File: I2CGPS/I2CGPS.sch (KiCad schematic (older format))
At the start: 9 parts, among them P1 CONN_01X05, P2 CONN_01X09, P3 CONN_01X09, Q1 BSS84, U1 GY-NEO6MV2

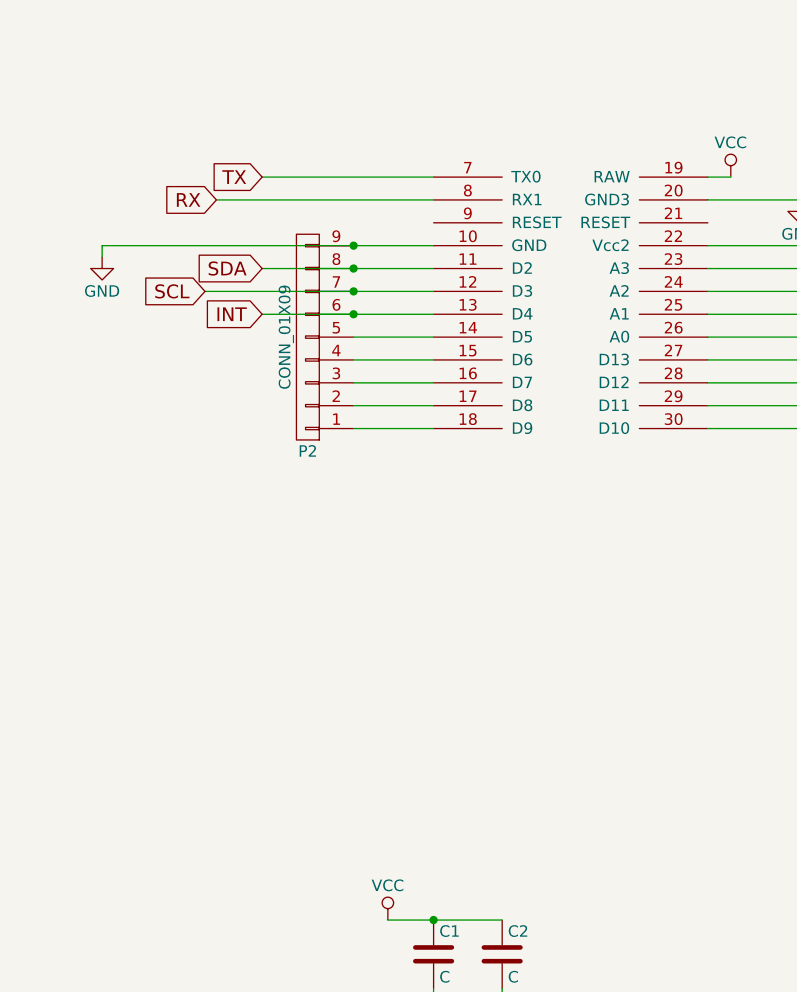
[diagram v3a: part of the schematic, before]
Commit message: added softserial to board
allows selection of hardware serial or soft serial by solder selector
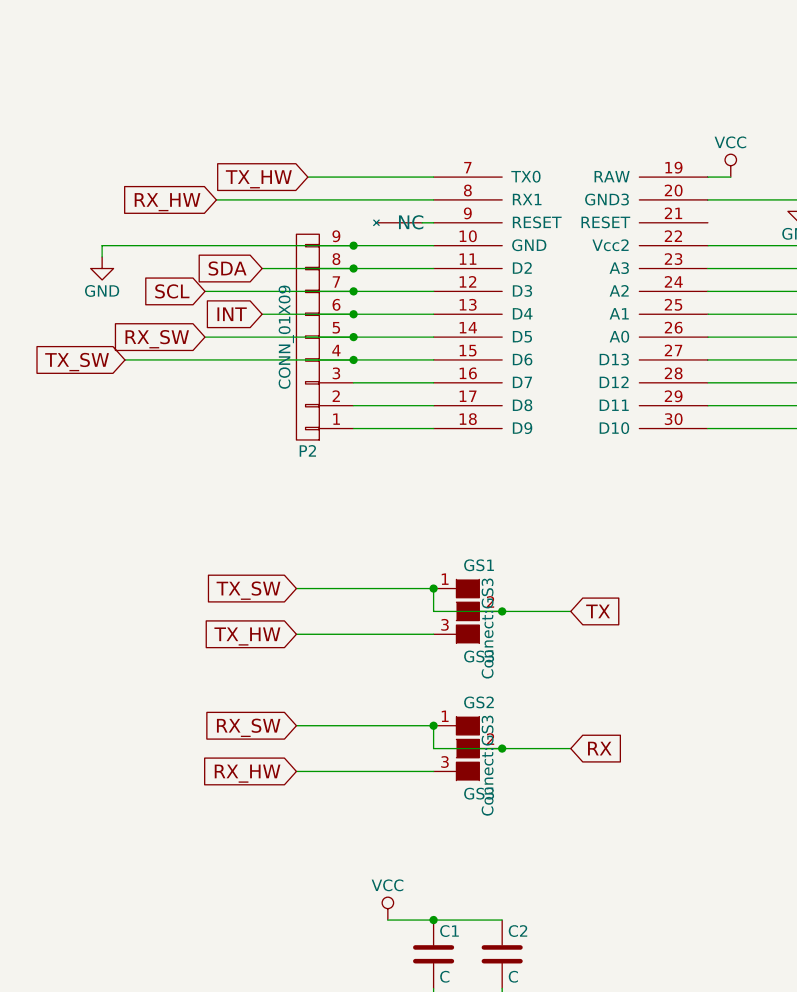
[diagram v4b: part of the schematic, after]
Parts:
- added GS1, GS2: GS3, Connect:GS3, symbol GS3
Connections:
- net RX: now also P2.5 (P5), uP1.14 (D5), GS2.1 (G1), GS2.2 (G2); no longer uP1.8 (RX1)
- net TX: now also P2.4 (P4), uP1.15 (D6), GS1.1 (G1), GS1.2 (G2); no longer uP1.7 (TX0)
- new net RX_HW: GS2.3 (G3), uP1.8 (RX1)
- new net TX_HW: GS1.3 (G3), uP1.7 (TX0)
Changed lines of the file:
@@
 	1    0    0    -1
 $EndComp
-Text GLabel 1450 3700 0    60   Input ~ 0
-TX
+Text GLabel 1650 3700 0    60   Input ~ 0
+TX_HW
 Text GLabel 1250 3800 0    60   Input ~ 0
-RX
+RX_HW
 Text GLabel 1450 4100 0    60   Input ~ 0
 SDA
@@
 	4950 3900 5250 3900
 Wire Wire Line
-	1450 3700 2200 3700
-Wire Wire Line
 	1250 3800 2200 3800
 Wire Wire Line
@@
 Wire Wire Line
 	3400 4000 4150 4000
-Wire Wire Line
-	750  4000 2200 4000
 Wire Wire Line
 	750  4000 750  4050
@@
 Wire Wire Line
 	2000 7300 2500 7300
-Wire Wire Line
-	2500 7300 2500 7250
 Connection ~ 2200 7300
 $Comp
@@
 Connection ~ 1850 4300
 Wire Wire Line
-	1850 4400 2200 4400
-Wire Wire Line
-	1850 4500 2200 4500
+	1200 4400 2200 4400
+Wire Wire Line
+	850  4500 2200 4500
 Wire Wire Line
 	2200 4600 1850 4600
@@
 Wire Wire Line
 	3500 3700 3400 3700
+Wire Wire Line
+	2500 7300 2500 7250
+$Comp
+L NC #U011
+U 1 1 5818CC7D
+P 2100 3900
+F 0 "#U011" H 1800 3950 60  0001 C CNN
+F 1 "NC" H 2100 3900 60  0000 C CNN
+F 2 "" H 2100 3900 60  0000 C CNN
+F 3 "" H 2100 3900 60  0000 C CNN
+	1    2100 3900
+	1    0    0    -1
+$EndComp
+Wire Wire Line
+	2200 3900 2150 3900
+Wire Wire Line
+	750  4000 2200 4000
+$Comp
+L GS3 GS2
+U 1 1 5818E038
+P 2350 6200
+F 0 "GS2" H 2400 6400 50  0000 C CNN
+F 1 "GS3" H 2400 6001 50  0000 C CNN
+F 2 "Connect:GS3" V 2438 6126 50  0000 C CNN
+F 3 "" H 2350 6200 50  0000 C CNN
+	1    2350 6200
+	1    0    0    -1
+$EndComp
+Text GLabel 2800 6200 2    60   Input ~ 0
+RX
+Text GLabel 1600 6100 0    60   Input ~ 0
+RX_SW
+Text GLabel 1600 6300 0    60   Input ~ 0
+RX_HW
+Wire Wire Line
+	2200 6200 2800 6200
+Wire Wire Line
+	1600 6100 2200 6100
+Wire Wire Line
+	2200 6300 1600 6300
+$Comp
+L GS3 GS1
+U 1 1 5818E30A
+P 2350 5600
+F 0 "GS1" H 2400 5800 50  0000 C CNN
+F 1 "GS3" H 2400 5401 50  0000 C CNN
+F 2 "Connect:GS3" V 2438 5526 50  0000 C CNN
+F 3 "" H 2350 5600 50  0000 C CNN
+	1    2350 5600
+	1    0    0    -1
+$EndComp
+Text GLabel 2800 5600 2    60   Input ~ 0
+TX
+Text GLabel 1600 5500 0    60   Input ~ 0
+TX_SW
+Text GLabel 1600 5700 0    60   Input ~ 0
+TX_HW
+Wire Wire Line
+	1600 5500 2200 5500
+Wire Wire Line
+	2200 5700 1600 5700
+Wire Wire Line
+	2200 5600 2800 5600
+Wire Wire Line
+	2200 3700 1650 3700
+Text GLabel 1200 4400 0    60   Input ~ 0
+RX_SW
+Text GLabel 850  4500 0    60   Input ~ 0
+TX_SW
+Connection ~ 1850 4400
+Connection ~ 1850 4500
+Wire Wire Line
+	2200 5500 2200 5600
+Connection ~ 2500 5600
+Wire Wire Line
+	2200 6100 2200 6200
+Connection ~ 2500 6200
+Connection ~ 2200 6100
+Connection ~ 2200 5500
 $EndSCHEMATC
